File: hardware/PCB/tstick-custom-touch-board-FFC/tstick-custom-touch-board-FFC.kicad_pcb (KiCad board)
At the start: 2 copper layers, 45.5 x 31.8 mm, 20 parts, among them IC1 CY8C206X6A

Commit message: added 3d models, minimised size of paper connector trill board, added pictures
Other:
- board text added: "Custom T-Stick Touch Board v0.0.1 2023-09-07 IDMIL McGill University"
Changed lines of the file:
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@@
   (gr_arc (start 106.28 77.875) (mid 107.15868 75.75368) (end 109.28 74.875)
     (stroke (width 0.1) (type default)) (layer "Edge.Cuts"))
+  (gr_text "Custom T-Stick Touch Board v0.0.1 2023-09-07\nIDMIL McGill University" (at 148.625 103.525) (layer "B.SilkS")
+    (effects (font (size 1 1) (thickness 0.15)) (justify left bottom mirror))
+  )
   (gr_text "0\n1" (at 128.4 84.85) (layer "F.SilkS")
     (effects (font (size 0.8 0.8) (thickness 0.15)) (justify left bottom))

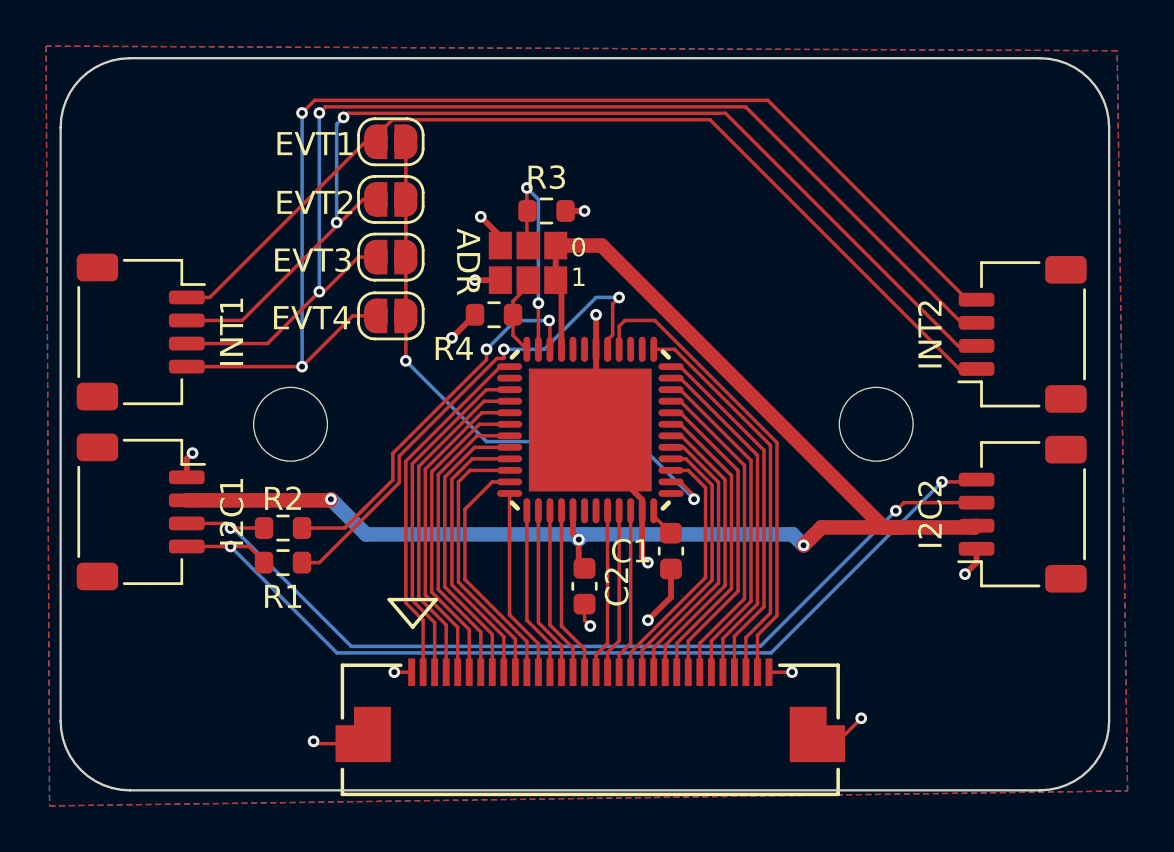
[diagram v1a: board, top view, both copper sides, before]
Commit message: removed libaries not related to projects, cleaned up global and project specific libraries, changed capsense controller to smaller 6x6mm package
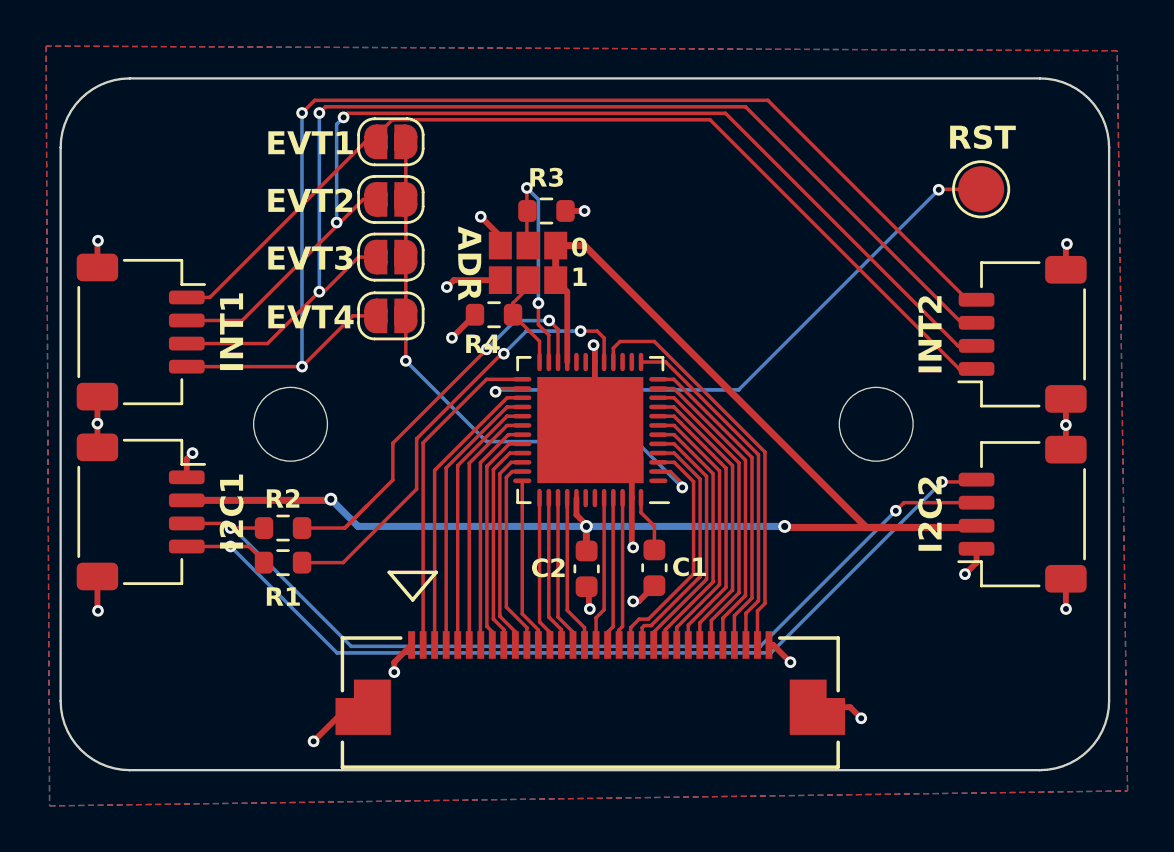
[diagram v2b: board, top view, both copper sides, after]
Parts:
- added J1: Conn_01x01, TestPoint:TestPoint_Pad_D2.0mm, F.Cu at (146.2, 80.6)
- FFC1: footprint molex-ffc-connectors:CON_541323262_MOL -> Molex_FFC Connector:CON_541323262_MOL
- I2C1, I2C2, INT1, INT2: footprint Connector_JST:JST_SH_SM04B-SRSS-TB_1x04-1MP_P1.00mm_Horizontal -> JST-footprints:JST_SH_SM04B-SRSS-TB_1x04-1MP_P1.00mm_Horizontal
- IC1: footprint cap-touch-breakout:QFN48-LEADS -> CY8C20646A-CY8C20636A-footprint:QFN-48_EP_6x6_Pitch0.4mm
- moved FFC1 1.18 mm to (129.2, 102.8)
- moved C1 1.02 mm to (132.0, 97.0)
- moved C2 0.76 mm to (129.1, 97.0)
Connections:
- net Net-(IC1-(INT)P0[1]) renamed /P01
- net Net-(IC1-(PR/SCL)P1[1]) renamed /PR/SCL
- net Net-(IC1-(PR/SDA)P1[0]) renamed /PR/SDA
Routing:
- net /RES: track 0.00 -> 25.8 mm, vias 0 -> 2
- net GND: track 27.8 -> 38.8 mm, vias 14 -> 20
- net /TOUCH5: track 13.1 -> 10.2 mm
- net /TOUCH6: track 12.7 -> 9.78 mm
- net /TOUCH7: track 12.2 -> 9.34 mm
- net /TOUCH8: track 11.7 -> 8.88 mm
- net /TOUCH4: track 13.6 -> 10.9 mm
- net /TOUCH29: track 20.4 -> 17.8 mm
- net /TOUCH3: track 14.1 -> 11.5 mm
- net /TOUCH2: track 14.5 -> 12.1 mm
- net /TOUCH1: track 15.0 -> 12.7 mm
- net /PR/SCL: track 21.9 -> 19.7 mm
- net /TOUCH9: track 10.6 -> 8.43 mm
- net +3V3: track 63.9 -> 61.8 mm
- net /TOUCH28: track 17.1 -> 15.2 mm
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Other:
- board size 45.5 x 31.8 mm -> 45.5 x 30 mm
- board text added: "Custom T-Stick Touch Board v0.0.1 2023-10 IDMIL McGill University"
- board text added: "RST"
- board text removed: "Custom T-Stick Touch Board v0.0.1 2023-09-07 IDMIL McGill University"

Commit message: removed dropped ideas, re organised datasheets, created project for integrated touch sensor
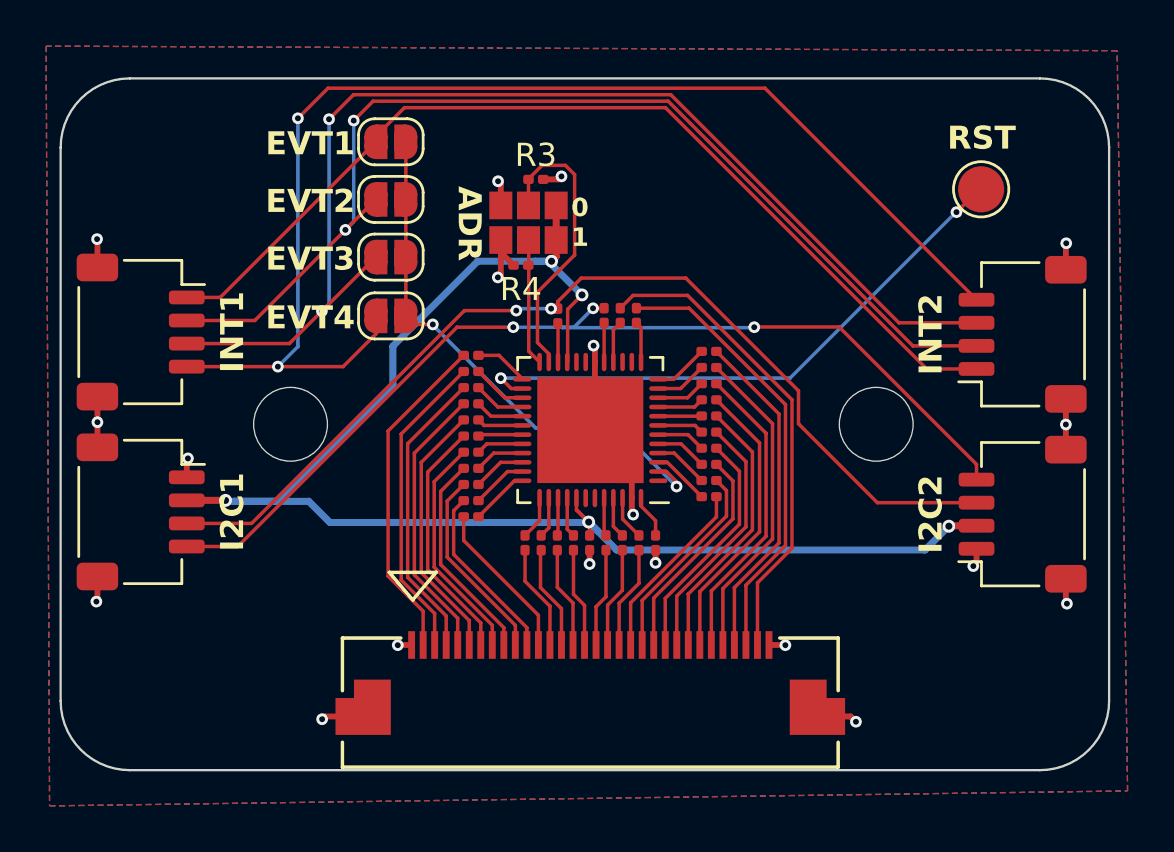
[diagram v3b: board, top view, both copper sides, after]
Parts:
- added R10: 560, Resistor_SMD:R_0201_0603Metric, F.Cu at (134.4, 90.4)
- added R11: 560, Resistor_SMD:R_0201_0603Metric, F.Cu at (134.4, 89.7)
- added R12: 560, Resistor_SMD:R_0201_0603Metric, F.Cu at (134.4, 89.0)
- added R13: 560, Resistor_SMD:R_0201_0603Metric, F.Cu at (134.4, 88.3)
- added R14: 560, Resistor_SMD:R_0201_0603Metric, F.Cu at (134.4, 87.6)
- added R15: 560, Resistor_SMD:R_0201_0603Metric, F.Cu at (131.2, 86.0)
- added R16: 560, Resistor_SMD:R_0201_0603Metric, F.Cu at (130.6, 86.0)
- added R17: 560, Resistor_SMD:R_0201_0603Metric, F.Cu at (124.1, 87.8)
- added R18: 560, Resistor_SMD:R_0201_0603Metric, F.Cu at (124.1, 88.5)
- added R19: 560, Resistor_SMD:R_0201_0603Metric, F.Cu at (124.1, 89.2)
- added R20: 560, Resistor_SMD:R_0201_0603Metric, F.Cu at (124.1, 89.9)
- added R21: 560, Resistor_SMD:R_0201_0603Metric, F.Cu at (124.1, 90.6)
- added R22: 560, Resistor_SMD:R_0201_0603Metric, F.Cu at (124.1, 91.3)
- added R23: 560, Resistor_SMD:R_0201_0603Metric, F.Cu at (124.1, 92.0)
- added R24: 560, Resistor_SMD:R_0201_0603Metric, F.Cu at (124.1, 92.7)
- added R25: 560, Resistor_SMD:R_0201_0603Metric, F.Cu at (124.1, 93.4)
- added R26: 560, Resistor_SMD:R_0201_0603Metric, F.Cu at (124.1, 94.1)
- added R27: 560, Resistor_SMD:R_0201_0603Metric, F.Cu at (124.1, 94.8)
- added R28: 560, Resistor_SMD:R_0201_0603Metric, F.Cu at (126.4, 95.9)
- added R29: 560, Resistor_SMD:R_0201_0603Metric, F.Cu at (127.1, 95.9)
- added R30: 560, Resistor_SMD:R_0201_0603Metric, F.Cu at (127.8, 95.9)
- added R31: 560, Resistor_SMD:R_0201_0603Metric, F.Cu at (128.5, 95.9)
- added R32: 560, Resistor_SMD:R_0201_0603Metric, F.Cu at (129.9, 95.9)
- added R33: 560, Resistor_SMD:R_0201_0603Metric, F.Cu at (130.6, 95.9)
- added R34: 560, Resistor_SMD:R_0201_0603Metric, F.Cu at (131.4, 95.9)
- added R5: 560, Resistor_SMD:R_0201_0603Metric, F.Cu at (134.4, 93.9)
- added R6: 560, Resistor_SMD:R_0201_0603Metric, F.Cu at (134.4, 93.2)
- added R7: 560, Resistor_SMD:R_0201_0603Metric, F.Cu at (134.4, 92.5)
- added R8: 560, Resistor_SMD:R_0201_0603Metric, F.Cu at (134.4, 91.8)
- added R9: 560, Resistor_SMD:R_0201_0603Metric, F.Cu at (134.4, 91.1)
- C1, C2: footprint Capacitor_SMD:C_0603_1608Metric -> Capacitor_SMD:C_0201_0603Metric
- R1, R2, R3, R4: footprint Resistor_SMD:R_0603_1608Metric -> Resistor_SMD:R_0201_0603Metric
- moved R1 17.6 mm to (129.8, 86.0), turned to -90 degrees
- moved R2 15.1 mm to (127.8, 86.1), turned to -90 degrees
- moved R4 2.45 mm to (126.2, 83.8)
- moved JP1A1 1.74 mm to (127.8, 81.3)
- moved JP1B1 1.74 mm to (127.8, 82.8)
- moved R3 1.45 mm to (126.9, 80.1)
- moved C2 1.14 mm to (129.2, 95.9)
- moved C1 1.09 mm to (132.1, 95.9)
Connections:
- IC1 pad 10: /TOUCH25 -> Net-(IC1-P3[3])
- IC1 pad 11: /TOUCH26 -> Net-(IC1-P3[1])
- IC1 pad 12: /TOUCH27 -> Net-(IC1-(SCL)P1[7])
- IC1 pad 13: /TOUCH28 -> Net-(IC1-(SDA)P1[5])
- IC1 pad 16: /TOUCH29 -> Net-(IC1-P1[3])
- IC1 pad 25: /TOUCH0 -> Net-(IC1-P1[6])
- IC1 pad 27: /TOUCH1 -> Net-(IC1-P3[0])
- IC1 pad 28: /TOUCH2 -> Net-(IC1-P3[2])
- IC1 pad 29: /TOUCH3 -> Net-(IC1-P3[4])
- IC1 pad 3: /TOUCH18 -> Net-(IC1-P2[5])
- IC1 pad 30: /TOUCH4 -> Net-(IC1-P3[6])
- IC1 pad 31: /TOUCH5 -> Net-(IC1-P4[0])
- IC1 pad 32: /TOUCH6 -> Net-(IC1-P4[2])
- IC1 pad 33: /TOUCH7 -> Net-(IC1-P2[0])
- IC1 pad 34: /TOUCH8 -> Net-(IC1-P2[2])
- IC1 pad 35: /TOUCH9 -> Net-(IC1-P2[4])
- IC1 pad 36: /TOUCH10 -> Net-(IC1-P2[6])
- IC1 pad 37: /TOUCH11 -> Net-(IC1-P0[0])
- IC1 pad 38: /TOUCH12 -> Net-(IC1-P0[2])
- IC1 pad 39: /TOUCH13 -> Net-(IC1-P0[4])
- IC1 pad 4: /TOUCH19 -> Net-(IC1-P2[3])
- IC1 pad 40: /TOUCH14 -> Net-(IC1-P0[6])
- IC1 pad 44: /TOUCH15 -> Net-(IC1-P0[7])
- IC1 pad 45: /TOUCH16 -> Net-(IC1-P0[5])
- IC1 pad 46: /TOUCH17 -> Net-(IC1-(INT)P0[3])
- IC1 pad 5: /TOUCH20 -> Net-(IC1-P2[1])
- IC1 pad 6: /TOUCH21 -> Net-(IC1-P4[3])
- IC1 pad 7: /TOUCH22 -> Net-(IC1-P4[1])
- IC1 pad 8: /TOUCH23 -> Net-(IC1-P3[7])
- IC1 pad 9: /TOUCH24 -> Net-(IC1-P3[5])
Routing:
- net /PR/SCL: track 19.7 -> 1.69 mm, vias 2 -> 0
- net /PR/SDA: track 18.7 -> 1.68 mm, vias 2 -> 0
- net GND: track 38.8 -> 29.4 mm, vias 20 -> 19
- net +3V3: track 61.8 -> 66.2 mm, vias 3 -> 5
- net /TOUCH28: track 15.2 -> 19.3 mm
- net /TOUCH29: track 17.8 -> 20.8 mm
- net /SDA: track 41.0 -> 43.7 mm
- net Net-(IC1-P2[6]): track 0.00 -> 2.55 mm
- net Net-(IC1-P2[5]): track 0.00 -> 2.50 mm
- net Net-(IC1-P2[4]): track 0.00 -> 2.42 mm
- net Net-(IC1-(SCL)P1[7]): track 0.00 -> 2.38 mm
- net Net-(IC1-P2[3]): track 0.00 -> 2.37 mm
- net Net-(IC1-P3[0]): track 0.00 -> 2.37 mm
- net /TOUCH14: track 6.68 -> 4.31 mm
- net /TOUCH18: track 10.3 -> 7.97 mm
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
